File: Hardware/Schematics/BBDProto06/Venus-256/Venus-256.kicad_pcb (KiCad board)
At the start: 2 copper layers, 172.7 x 109.2 mm, 223 parts, among them J201 RaspberryPi header, J301 ARM JTAG, U1001 AD7616, U101 ADG715, U401 AD7616, U501 ATSAME70Q21A-AN, U601 AD7616, U701 AD7616, U801 AD7616, U901 ATSAME70Q21A-AN

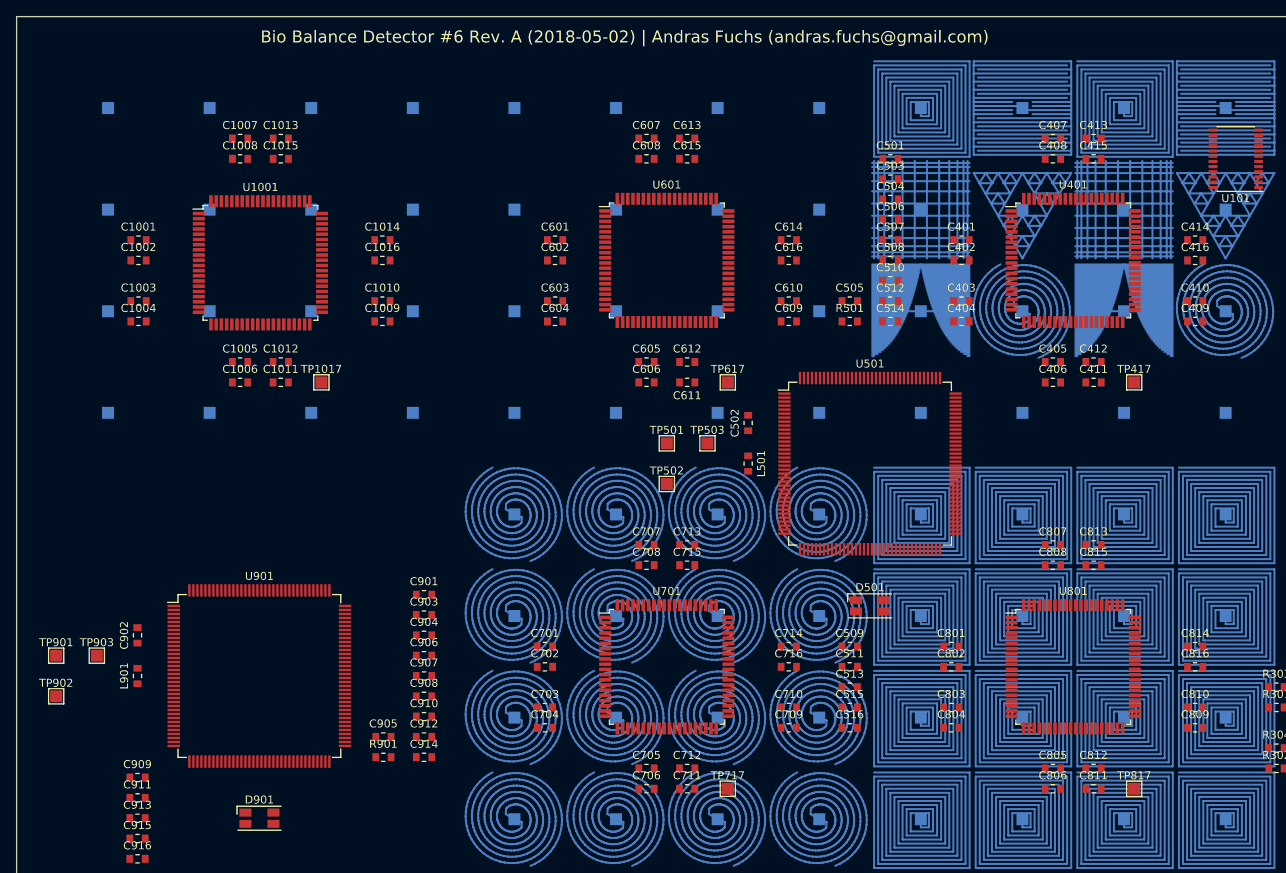
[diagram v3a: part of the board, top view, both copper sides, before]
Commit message: Added all antennas
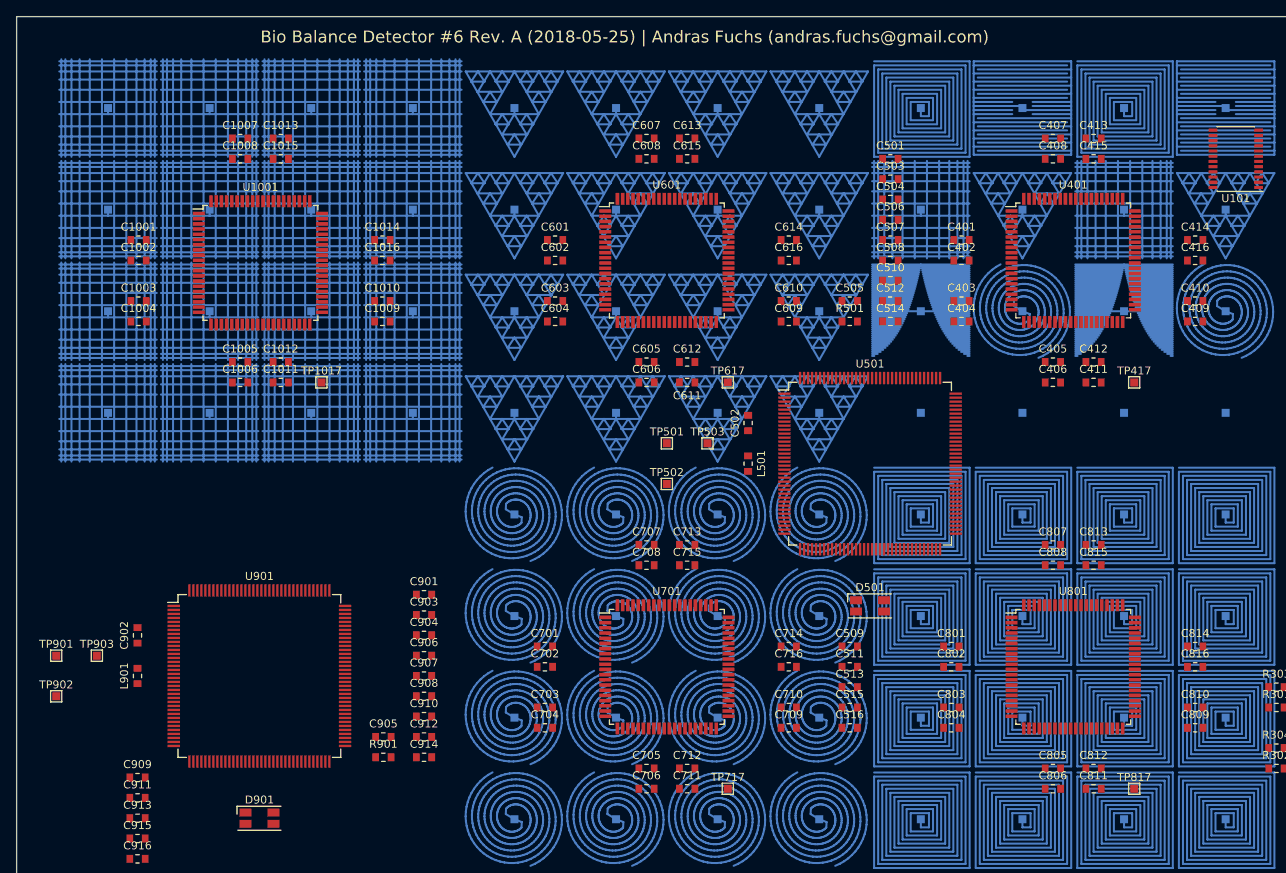
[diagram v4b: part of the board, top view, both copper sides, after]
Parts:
- TP1001, TP1002, TP1003, TP1004, TP1005, TP1006, TP1007, TP1008, TP1009, TP1010, TP1011, TP1012, TP1013, TP1014, TP1015, TP1016, TP1017, TP401, TP402, TP403, TP404, TP405, TP406, TP407, TP408, TP409, TP410, TP411, TP412, TP413, TP414, TP415, TP416, TP417, TP501, TP502, TP503, TP601, TP602, TP603, TP604, TP605, TP606, TP607, TP608, TP609, TP610, TP611, TP612, TP613, TP614, TP615, TP616, TP617, TP701, TP702, TP703, TP704, TP705, TP706, TP707, TP708, TP709, TP710, TP711, TP712, TP713, TP714, TP715, TP716, TP717, TP801, TP802, TP803, TP804, TP805, TP806, TP807, TP808, TP809, TP810, TP811, TP812, TP813, TP814, TP815, TP816, TP817, TP901, TP902, TP903: footprint TestPoint:TestPoint_Pad_1.5x1.5mm -> TestPoint:TestPoint_Pad_1.0x1.0mm
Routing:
- net Net-(TP408-Pad1): track 292.6 -> 4780.0 mm
- net Net-(TP405-Pad1): track 125.1 -> 878.4 mm
- net Net-(TP612-Pad1): track 0.00 -> 78.8 mm
- net Net-(TP601-Pad1): track 0.00 -> 78.8 mm
- net Net-(TP616-Pad1): track 0.00 -> 78.8 mm
- net Net-(TP615-Pad1): track 0.00 -> 78.8 mm
- net Net-(TP614-Pad1): track 0.00 -> 78.8 mm
- net Net-(TP611-Pad1): track 0.00 -> 78.8 mm
- net Net-(TP604-Pad1): track 0.00 -> 78.8 mm
- net Net-(TP602-Pad1): track 0.00 -> 78.8 mm
- net Net-(TP608-Pad1): track 0.00 -> 78.8 mm
- net Net-(TP607-Pad1): track 0.00 -> 78.8 mm
- net Net-(TP606-Pad1): track 0.00 -> 78.8 mm
- net Net-(TP603-Pad1): track 0.00 -> 78.8 mm
- net Net-(TP610-Pad1): track 0.00 -> 78.8 mm
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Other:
- board text added: "Bio Balance Detector #6 Rev. A (2018-05-25) | Andras Fuchs (andras.fuchs@gmail.com)"
- board text removed: "Bio Balance Detector #6 Rev. A (2018-05-02) | Andras Fuchs (andras.fuchs@gmail.com)"

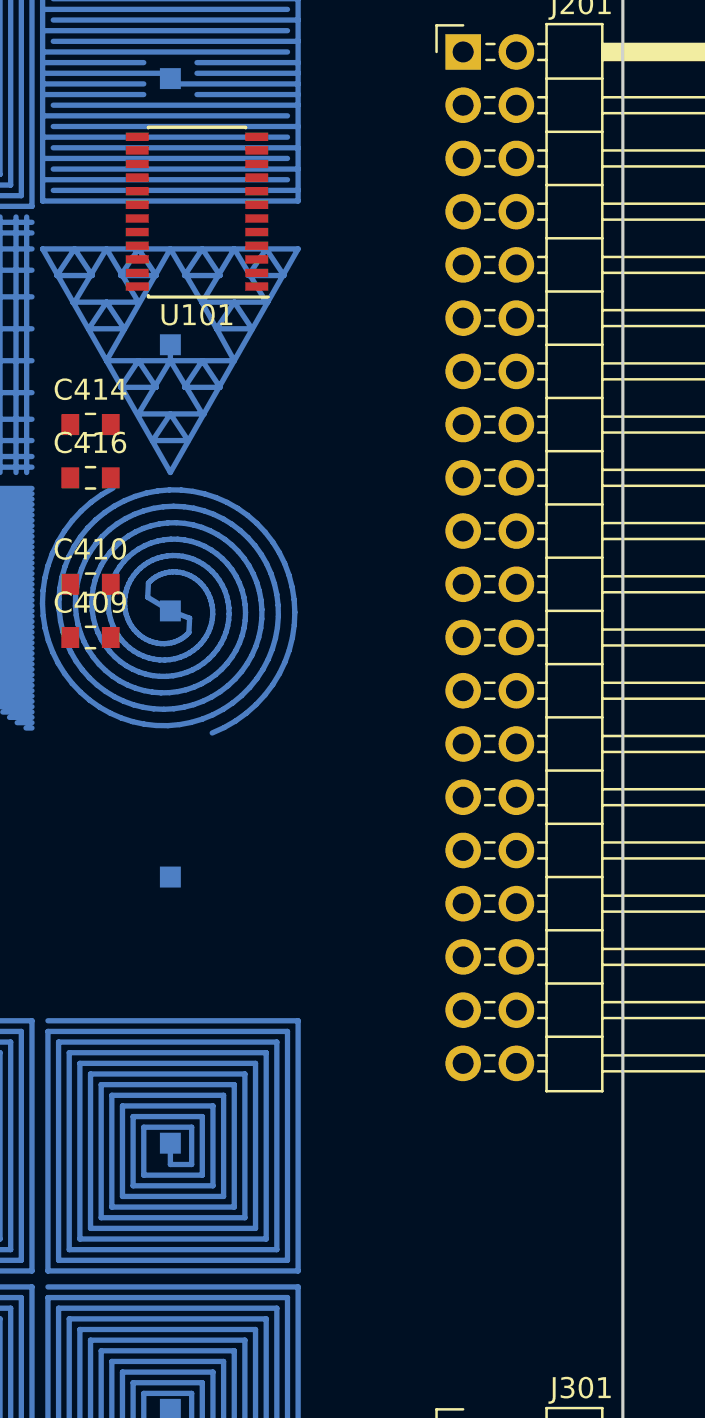
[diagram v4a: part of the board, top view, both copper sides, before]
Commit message: Replaced the ADG715 with TPS22993
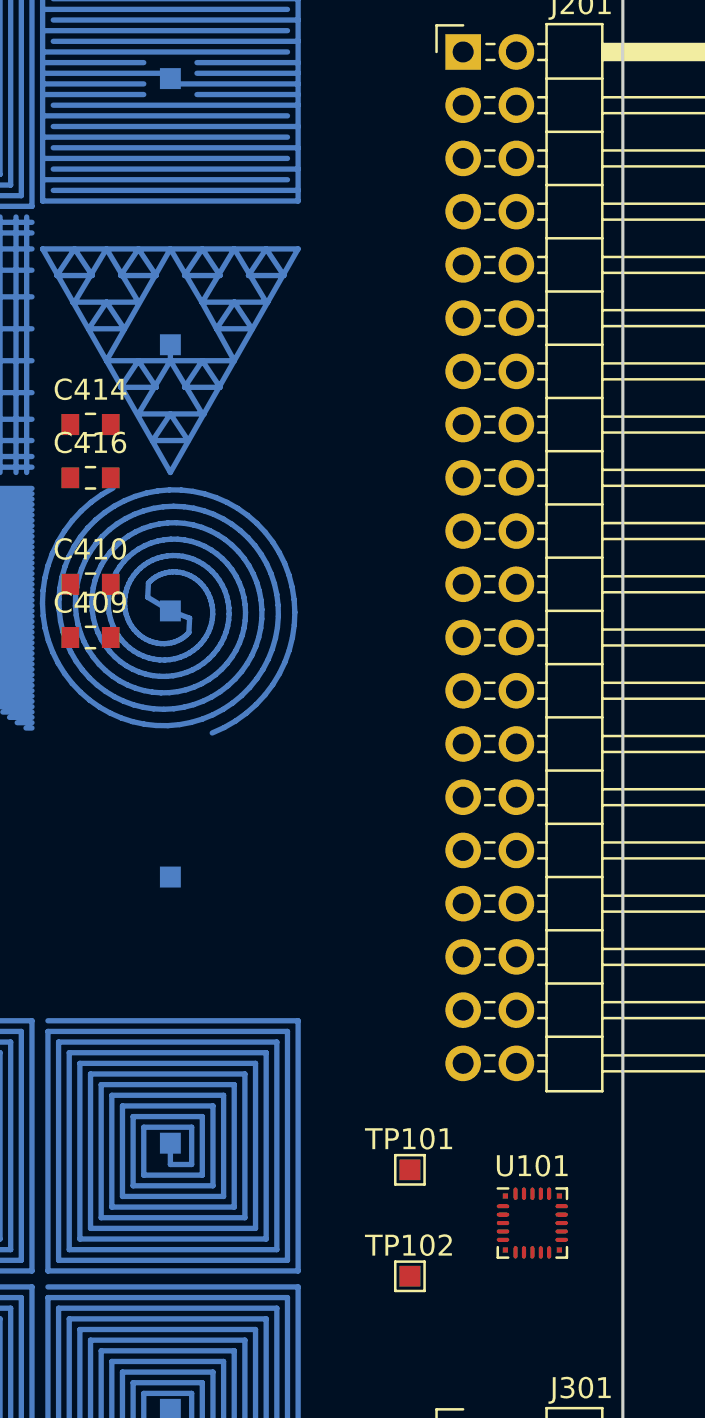
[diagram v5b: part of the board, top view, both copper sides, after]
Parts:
- added TP101: VOUT3_TP, TestPoint:TestPoint_Pad_1.0x1.0mm, F.Cu at (177.8, 78.7)
- added TP102: VOUT4_TP, TestPoint:TestPoint_Pad_1.0x1.0mm, F.Cu at (177.8, 83.8)
- U101: value ADG715 -> TPS22993; footprint Package_SO:TSSOP-24_4.4x7.8mm_P0.65mm -> Package_DFN_QFN:Texas_S-PWQFN-N20
- moved U101 50.8 mm to (183.6, 81.3), turned to 0 degrees
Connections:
- U101 pad 1: /RaspberryPiGPIOHeader/I2C_SCL1 -> /CellMaster-02/VCC_MCU_P3V3
- U101 pad 10: (no net) -> /RaspberryPiGPIOHeader/DC_POWER_3V3
- U101 pad 11: /RaspberryPiGPIOHeader/DC_POWER_3V3 -> Net-(TP102-Pad1)
- U101 pad 12: (no net) -> /RaspberryPiGPIOHeader/DC_POWER_3V3
- U101 pad 13: (no net) -> GND
- U101 pad 15: (no net) -> Net-(TP101-Pad1)
- U101 pad 16: /RaspberryPiGPIOHeader/DC_POWER_3V3 -> GND
- U101 pad 17: (no net) -> /RaspberryPiGPIOHeader/I2C_SCL1
- U101 pad 19: (no net) -> /RaspberryPiGPIOHeader/I2C_SDA1
- U101 pad 20: /RaspberryPiGPIOHeader/DC_POWER_3V3 -> GND
- U101 pad 3: /RaspberryPiGPIOHeader/I2C_SDA1 -> /RaspberryPiGPIOHeader/DC_POWER_5V0
- U101 pad 4: GND -> /RaspberryPiGPIOHeader/DC_POWER_3V3
- U101 pad 5: /RaspberryPiGPIOHeader/DC_POWER_3V3 -> /CellMaster-01/VCC_MCU_P3V3
- U101 pad 6: /CellMaster-01/VCC_MCU_P3V3 -> GND
- U101 pad 8: /CellMaster-02/VCC_MCU_P3V3 -> /RaspberryPiGPIOHeader/DC_POWER_3V3

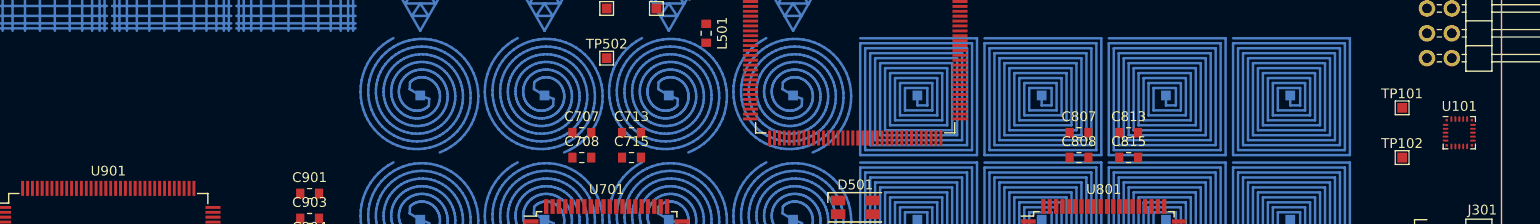
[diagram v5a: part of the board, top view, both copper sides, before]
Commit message: Moved the TPS22993
Moved the TPS22993
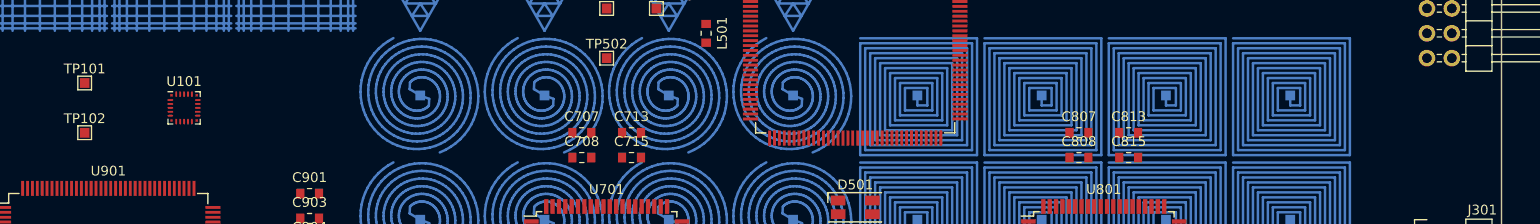
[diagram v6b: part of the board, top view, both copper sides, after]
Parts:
- moved TP101 134.6 mm to (43.2, 76.2)
- moved TP102 134.6 mm to (43.2, 81.3)
- moved U101 130.3 mm to (53.3, 78.7)
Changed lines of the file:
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@@
   )
   (module TestPoint:TestPoint_Pad_1.0x1.0mm (layer F.Cu)
-    (at 177.8 78.74)
+    (at 43.18 76.2)
     (descr "SMD rectangular pad as test Point, square 1.0mm side length")
     (tags "test point SMD pad rectangle square")
@@
   )
   (module TestPoint:TestPoint_Pad_1.0x1.0mm (layer F.Cu)
-    (at 177.8 83.82)
+    (at 43.18 81.28)
     (descr "SMD rectangular pad as test Point, square 1.0mm side length")
     (tags "test point SMD pad rectangle square")
@@
   )
   (module Package_DFN_QFN:Texas_S-PWQFN-N20 (layer F.Cu)
-    (at 183.642 81.28)
+    (at 53.34 78.74)
     (descr "20-Pin Plastic Quad Flatpack No-Lead Package, Body 3.0x3.0x0.8mm, Texas Instruments (http://www.ti.com/lit/ds/symlink/tps22993.pdf)")
     (tags "QFN 0.4")

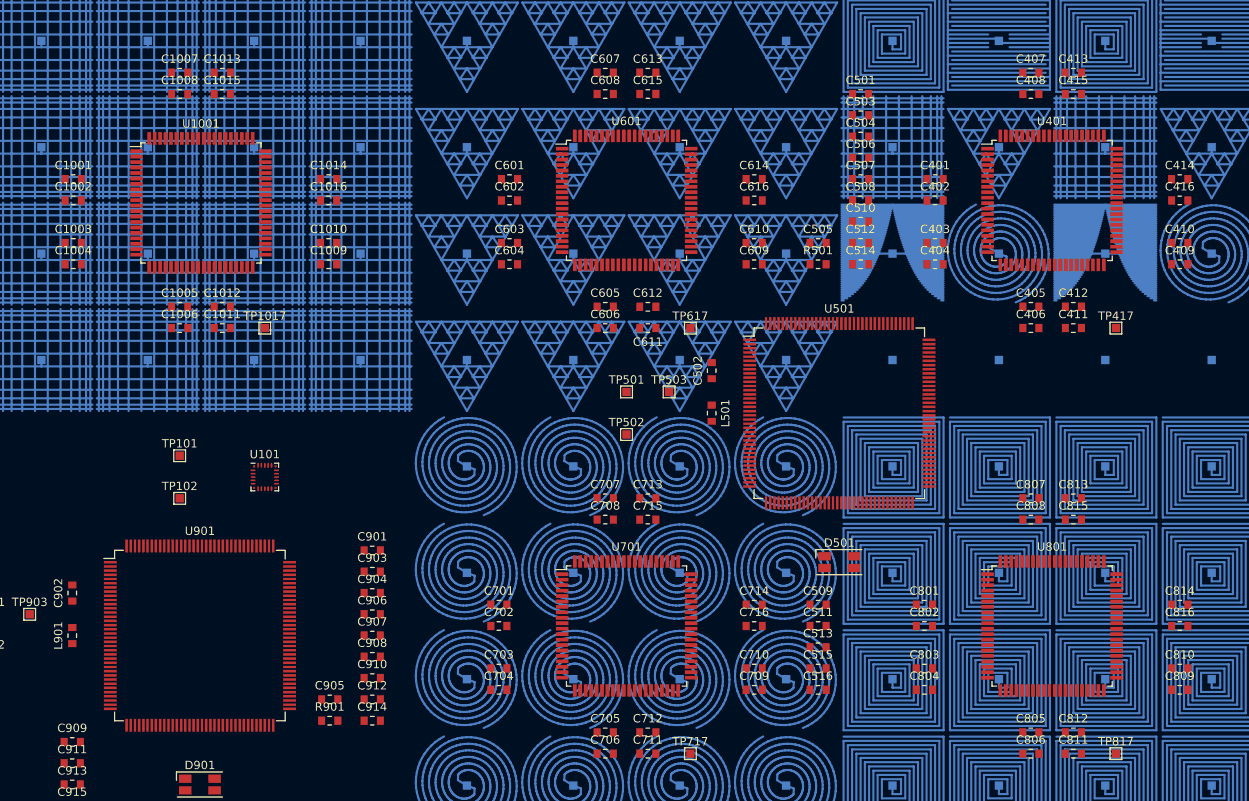
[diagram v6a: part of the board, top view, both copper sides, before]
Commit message: Updated the AD7616 symbol to match the library
Updated the AD7616 symbol to match the library
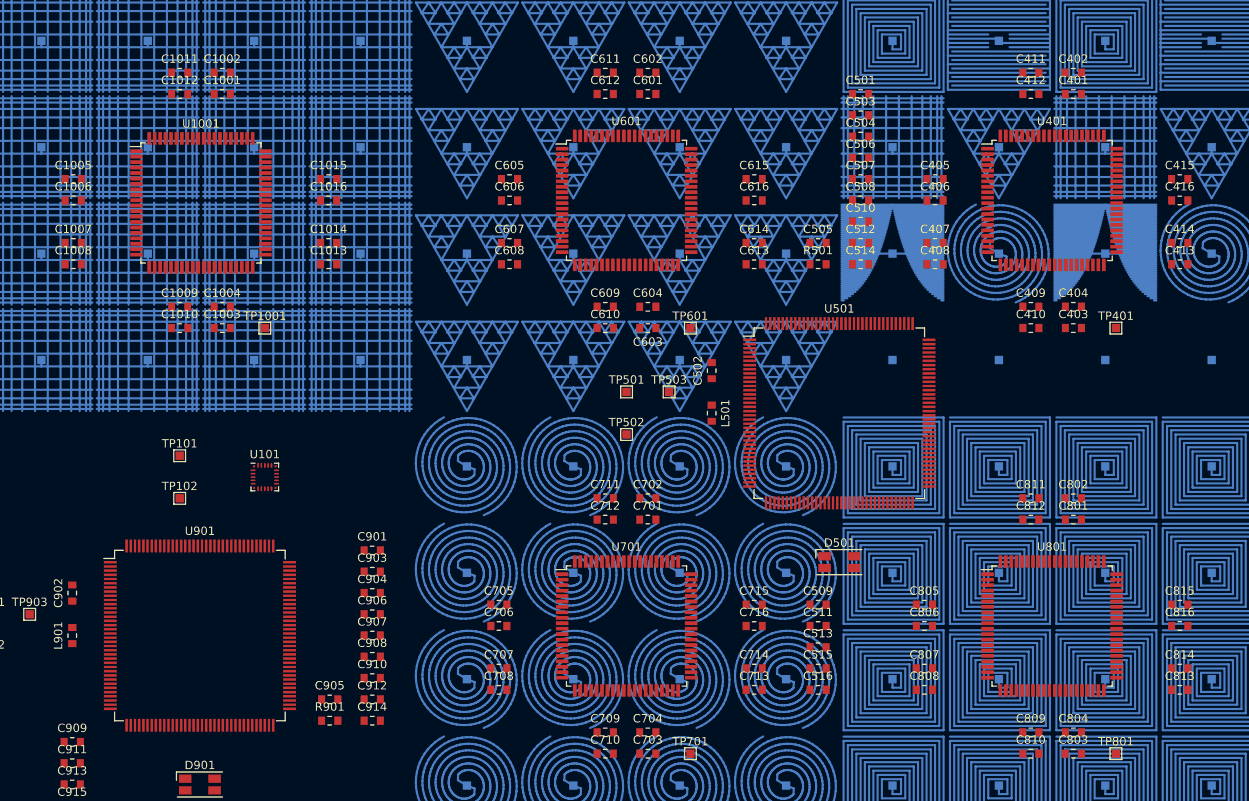
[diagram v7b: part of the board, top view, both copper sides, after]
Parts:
- renumbered C1015 to C1001, C1013 to C1002, C1011 to C1003, C1012 to C1004, C1001 to C1005, C1002 to C1006, C1003 to C1007, C1004 to C1008, C1005 to C1009, C1006 to C1010, C1007 to C1011, C1008 to C1012, C1009 to C1013, C1010 to C1014, C1014 to C1015, C415 to C401, C413 to C402, C411 to C403, C412 to C404, C401 to C405, C402 to C406, C403 to C407, C404 to C408, C405 to C409, C406 to C410, C407 to C411, C408 to C412, C409 to C413, C410 to C414, C414 to C415, C615 to C601, C613 to C602, C611 to C603, C612 to C604, C601 to C605, C602 to C606, C603 to C607, C604 to C608, C605 to C609, C606 to C610, C607 to C611, C608 to C612, C609 to C613, C610 to C614, C614 to C615, C715 to C701, C713 to C702, C711 to C703, C712 to C704, C701 to C705, C702 to C706, C703 to C707, C704 to C708, C705 to C709, C706 to C710, C707 to C711, C708 to C712, C709 to C713, C710 to C714, C714 to C715, C815 to C801, C813 to C802, C811 to C803, C812 to C804, C801 to C805, C802 to C806, C803 to C807, C804 to C808, C805 to C809, C806 to C810, C807 to C811, C808 to C812, C809 to C813, C810 to C814, C814 to C815, TP1017 to TP1001, TP1001 to TP1002, TP1002 to TP1003, TP1003 to TP1004, TP1004 to TP1005, TP1005 to TP1006, TP1006 to TP1007, TP1007 to TP1008, TP1008 to TP1009, TP1009 to TP1010, TP1010 to TP1011, TP1011 to TP1012, TP1012 to TP1013, TP1013 to TP1014, TP1014 to TP1015, TP1015 to TP1016, TP1016 to TP1017, TP417 to TP401, TP401 to TP402, TP402 to TP403, TP403 to TP404, TP404 to TP405, TP405 to TP406, TP406 to TP407, TP407 to TP408, TP408 to TP409, TP409 to TP410, TP410 to TP411, TP411 to TP412, TP412 to TP413, TP413 to TP414, TP414 to TP415, TP415 to TP416, TP416 to TP417, TP617 to TP601, TP601 to TP602, TP602 to TP603, TP603 to TP604, TP604 to TP605, TP605 to TP606, TP606 to TP607, TP607 to TP608, TP608 to TP609, TP609 to TP610, TP610 to TP611, TP611 to TP612, TP612 to TP613, TP613 to TP614, TP614 to TP615, TP615 to TP616, TP616 to TP617, TP717 to TP701, TP701 to TP702, TP702 to TP703, TP703 to TP704, TP704 to TP705, TP705 to TP706, TP706 to TP707, TP707 to TP708, TP708 to TP709, TP709 to TP710, TP710 to TP711, TP711 to TP712, TP712 to TP713, TP713 to TP714, TP714 to TP715, TP715 to TP716, TP716 to TP717, TP817 to TP801, TP801 to TP802, TP802 to TP803, TP803 to TP804, TP804 to TP805, TP805 to TP806, TP806 to TP807, TP807 to TP808, TP808 to TP809, TP809 to TP810, TP810 to TP811, TP811 to TP812, TP812 to TP813, TP813 to TP814, TP814 to TP815, TP815 to TP816, TP816 to TP817
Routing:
- net Net-(TP409-Pad1): track 4780.0 -> 13.0 mm
- net Net-(TP408-Pad1): track 125.8 -> 4845.9 mm
- net Net-(TP405-Pad1): track 300.2 -> 1099.8 mm
- net Net-(TP406-Pad1): track 878.4 -> 359.2 mm
- net Net-(TP412-Pad1): track 154.0 -> 525.9 mm
- net Net-(TP413-Pad1): track 384.1 -> 12.2 mm
- net Net-(TP411-Pad1): track 384.1 -> 12.2 mm
- net Net-(TP410-Pad1): track 154.0 -> 525.9 mm
- net Net-(TP407-Pad1): track 293.4 -> 60.0 mm
